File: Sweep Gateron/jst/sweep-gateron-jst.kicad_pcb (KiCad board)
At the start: 2 copper layers, 229.5 x 95.2 mm, 61 parts, among them SW10 SW_Push, SW10_r1 SW_Push, SW11 SW_Push, SW11_r1 SW_Push, SW12 SW_Push, SW12_r1 SW_Push, SW13_r1 SW_Push, SW14 SW_Push, SW14_r1 SW_Push, SW15 SW_Push, SW15_r1 SW_Push, SW16 SW_Push, SW16_r1 SW_Push, SW17 SW_Push, SW18 SW_Push, SW2 SW_Push, SW2 SW_SPDT, SW20 SW_Push, SW21 SW_Push, SW2_r1 SW_Push, SW3 SW_Push, SW3_r1 SW_Push, SW4 SW_Push, SW4_r1 SW_Push, SW5 SW_Push, SW5_r1 SW_Push, SW6 SW_Push, SW6_r1 SW_Push, SW7_r1 SW_Push, SW8 SW_Push, SW8_r1 SW_Push, SW9 SW_Push, SW9_r1 SW_Push, U1 ProMicro-kbd, U2 ProMicro-kbd

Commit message: Added gerber files
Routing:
- net gnd: vias 33 -> 34
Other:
- board text added: "There is no prize to perfection, only an end to pursuit"
- board text removed: "The Aeroplane Flies High (Turns Left, Looks Right)"
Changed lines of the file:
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@@
 		)
 		(fp_text user "RESET"
-			(at 0 2.286 90)
-			(layer "B.SilkS")
+			(at 0 -1.2 90)
+			(layer "F.SilkS")
 			(effects
 				(font
@@
 		)
 		(fp_text user "RESET"
-			(at 0 2.286 90)
-			(layer "B.SilkS")
+			(at 0 1.7 90)
+			(layer "F.SilkS")
 			(effects
 				(font
@@
 	(gr_text "Face down"
 		(at 160.10984 99.23 90)
-		(layer "F.SilkS")
-		(effects
-			(font
-				(size 1.5 1.5)
-				(thickness 0.3)
-			)
-		)
-	)
-	(gr_text "Face down"
-		(at 139.7 99.06 90)
-		(layer "F.SilkS")
+		(layer "B.SilkS")
 		(effects
 			(font
@@
 		)
 	)
-	(gr_text "The Aeroplane Flies High (Turns Left, Looks Right)"
-		(at 233.62984 122.936 0)
+	(gr_text "There is no prize to perfection, only an end to pursuit"
+		(at 232 123 0)
 		(layer "B.SilkS")
 		(effects
@@
 		)
 	)
+	(gr_text "Face down"
+		(at 139.7 99.06 90)
+		(layer "B.SilkS")
+		(effects
+			(font
+				(size 1.5 1.5)
+				(thickness 0.3)
+			)
+		)
+	)
 	(segment
-		(start 158.381843 85.323001)
-		(end 157.231843 84.173001)
+		(start 160.10984 86.585)
+		(end 160.12184 86.573)
+		(width 0.25)
+		(layer "F.Cu")
+		(net 1)
+	)
+	(segment
+		(start 160.10984 88.054)
+		(end 160.10984 86.585)
 		(width 0.25)
 		(layer "F.Cu")
@@
 	)
 	(segment
-		(start 157.231843 84.173001)
-		(end 155.720841 84.173001)
+		(start 157.558842 84.5)
+		(end 156.04784 84.5)
 		(width 0.25)
 		(layer "F.Cu")
@@
 	)
 	(segment
-		(start 155.720841 84.173001)
+		(start 156.04784 84.5)
 		(end 155.02984 83.482)
 		(width 0.25)
@@
 	)
 	(segment
-		(start 160.10984 86.585)
-		(end 160.12184 86.573)
+		(start 159.746841 85.323001)
+		(end 158.381843 85.323001)
 		(width 0.25)
 		(layer "F.Cu")
@@
 	)
 	(segment
-		(start 160.12184 85.698)
-		(end 159.746841 85.323001)
+		(start 159 115.920799)
+		(end 159 92)
 		(width 0.25)
 		(layer "F.Cu")
@@
 	)
 	(segment
-		(start 159.746841 85.323001)
-		(end 158.381843 85.323001)
+		(start 159 92)
+		(end 155.5 88.5)
 		(width 0.25)
 		(layer "F.Cu")
@@
 	)
 	(segment
-		(start 160.10984 88.054)
-		(end 160.10984 86.585)
+		(start 158.381843 85.323001)
+		(end 157.558842 84.5)
 		(width 0.25)
 		(layer "F.Cu")
@@
 	)
 	(segment
-		(start 160.12184 86.573)
-		(end 160.12184 85.698)
+		(start 160.12184 85.698)
+		(end 159.746841 85.323001)
 		(width 0.25)
 		(layer "F.Cu")
@@
 	)
 	(segment
-		(start 155.02984 88.02984)
+		(start 155.5 83.952162)
 		(end 155.02984 83.482002)
 		(width 0.25)
@@
 	)
 	(segment
-		(start 159 115.920799)
-		(end 159 92)
+		(start 155.5 88.5)
+		(end 155.5 83.952162)
 		(width 0.25)
 		(layer "F.Cu")
@@
 	)
 	(segment
-		(start 157.1527 117.768099)
-		(end 159 115.920799)
+		(start 160.12184 86.573)
+		(end 160.12184 85.698)
 		(width 0.25)
 		(layer "F.Cu")
@@
 	)
 	(segment
-		(start 159 92)
-		(end 155.02984 88.02984)
+		(start 157.1527 117.768099)
+		(end 159 115.920799)
 		(width 0.25)
 		(layer "F.Cu")
@@
 		(size 0.8)
 		(drill 0.4)
+		(layers "F.Cu" "B.Cu")
+		(free yes)
+		(net 2)
+	)
+	(via
+		(at 137.5 90)
+		(size 0.8)
+		(drill 0.4)

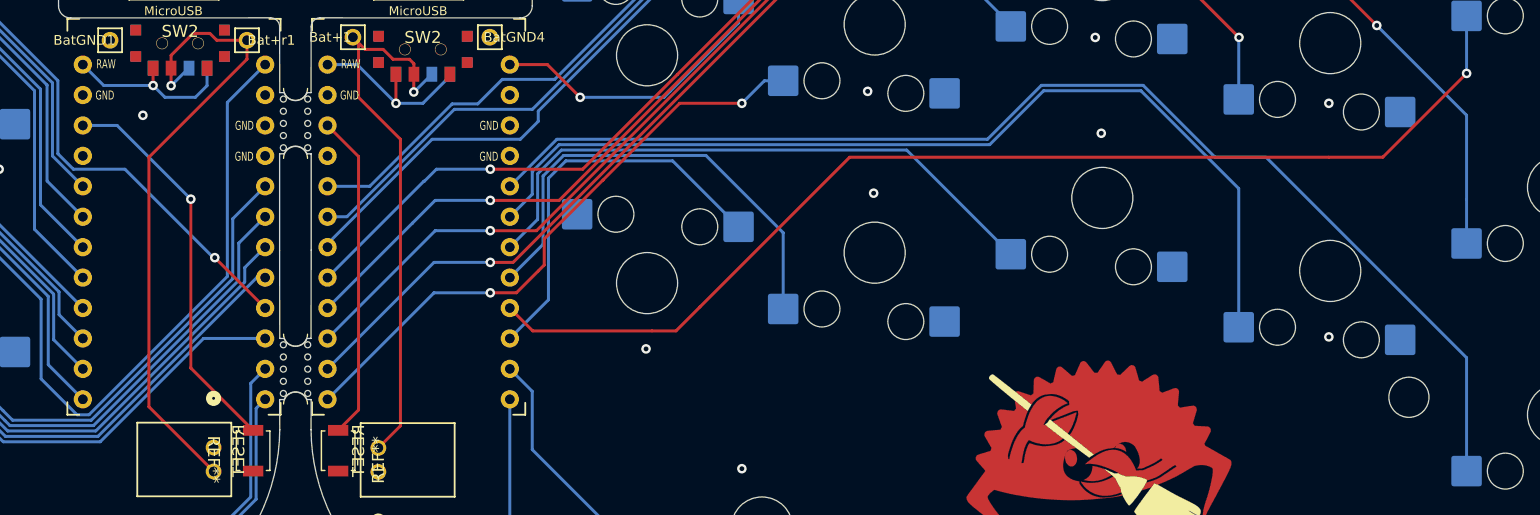
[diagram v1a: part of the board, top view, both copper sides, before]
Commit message: Fixed swapped pads and generated gerber files
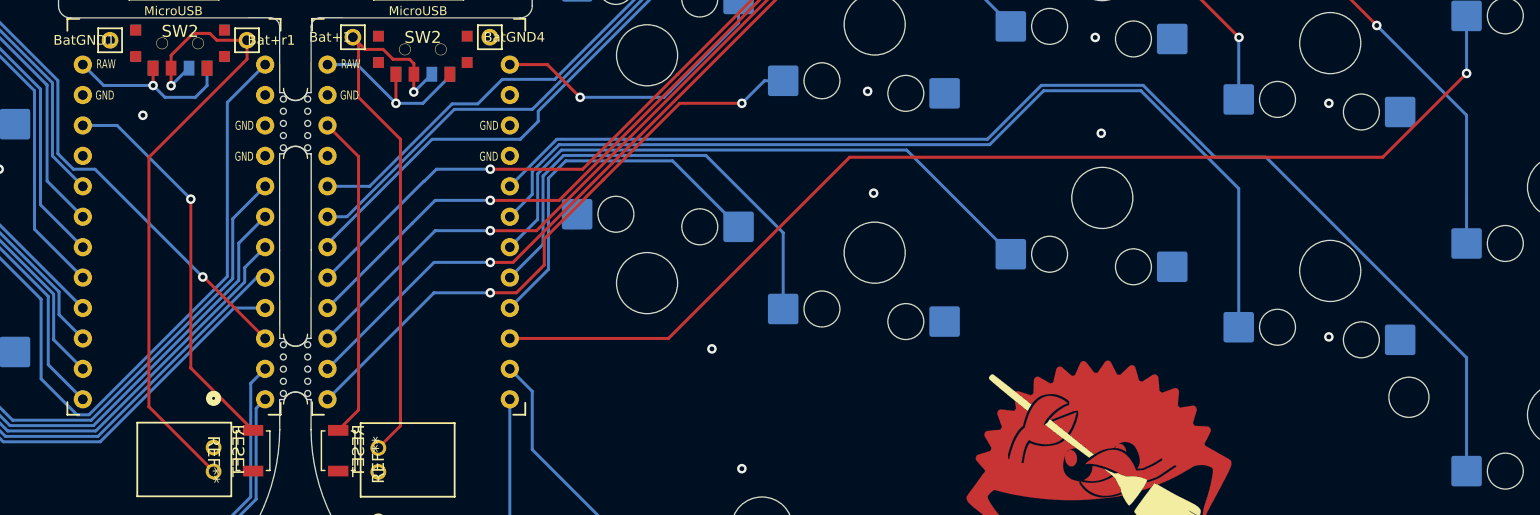
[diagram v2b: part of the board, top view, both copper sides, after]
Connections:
- U1 pad 10: Switch15 -> Switch1
- U1 pad 9: Switch1 -> Switch15
- U2 pad 10: Switch15_r -> Switch1_r
- U2 pad 9: Switch1_r -> Switch15_r
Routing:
- net Switch15_r: track 33.5 -> 30.9 mm
- net Switch1: track 128.1 -> 129.2 mm
- net Switch15: track 41.5 -> 42.5 mm
- net Switch1_r: track 94.4 -> 93.8 mm
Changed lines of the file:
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@@
 			(layers "*.Cu" "B.Mask" "F.SilkS")
 			(remove_unused_layers no)
-			(net 6 "Switch1")
+			(net 20 "Switch15")
 			(pinfunction "D7")
 			(pintype "bidirectional")
@@
 			(layers "*.Cu" "B.Mask" "F.SilkS")
 			(remove_unused_layers no)
-			(net 20 "Switch15")
+			(net 6 "Switch1")
 			(pinfunction "E6")
 			(pintype "bidirectional")
@@
 			(layers "*.Cu" "B.Mask" "F.SilkS")
 			(remove_unused_layers no)
-			(net 36 "Switch1_r")
+			(net 33 "Switch15_r")
 			(pinfunction "D7")
 			(pintype "bidirectional")
@@
 			(layers "*.Cu" "B.Mask" "F.SilkS")
 			(remove_unused_layers no)
-			(net 33 "Switch15_r")
+			(net 36 "Switch1_r")
 			(pinfunction "E6")
 			(pintype "bidirectional")
@@
 	)
 	(via
-		(at 179.5 109.5)
+		(at 185 109.5)
 		(size 0.8)
 		(drill 0.4)
@@
 	)
 	(segment
-		(start 143.5 101.8826)
-		(end 147.7054 106.088)
+		(start 142.5 103.5)
+		(end 142.5774 103.5)
+		(width 0.25)
+		(layer "F.Cu")
+		(net 6)
+	)
+	(segment
+		(start 142.5774 103.5)
+		(end 147.7054 108.628)
 		(width 0.25)
 		(layer "F.Cu")
@@
 	)
 	(via
-		(at 143.5 101.8826)
+		(at 142.5 103.5)
 		(size 0.8)
 		(drill 0.4)
@@
 	)
 	(segment
-		(start 136 94.5)
-		(end 131.69521 94.5)
-		(width 0.25)
-		(layer "B.Cu")
-		(net 6)
-	)
-	(segment
 		(start 61.663082 61.5)
 		(end 52.6375 70.525582)
@@
 	)
 	(segment
+		(start 133.5 94.5)
+		(end 142.5 103.5)
+		(width 0.25)
+		(layer "B.Cu")
+		(net 6)
+	)
+	(segment
 		(start 84.836935 66.5)
 		(end 79.836935 61.5)
@@
 	)
 	(segment
-		(start 143.3826 101.8826)
-		(end 136 94.5)
-		(width 0.25)
-		(layer "B.Cu")
-		(net 6)
-	)
-	(segment
 		(start 130.402 93.20679)
 		(end 130.402 87.10169)
@@
 	)
 	(segment
-		(start 143.5 101.8826)
-		(end 143.3826 101.8826)
+		(start 52.6375 70.525582)
+		(end 52.6375 72.3)
 		(width 0.25)
 		(layer "B.Cu")
@@
 	)
 	(segment
-		(start 52.6375 70.525582)
-		(end 52.6375 72.3)
+		(start 131.69521 94.5)
+		(end 130.402 93.20679)
 		(width 0.25)
 		(layer "B.Cu")
@@
 	(segment
 		(start 131.69521 94.5)
-		(end 130.402 93.20679)
+		(end 133.5 94.5)
 		(width 0.25)
 		(layer "B.Cu")
@@
 	)
 	(segment
-		(start 125.84157 117.255)
-		(end 133.93405 117.255)
+		(start 119.58657 111)
+		(end 125.84157 117.255)
 		(width 0.25)
 		(layer "B.Cu")
@@
 	)
 	(segment
-		(start 115.6345 111)
-		(end 119.58657 111)
+		(start 133.93405 117.255)
+		(end 145.10105 106.088)
 		(width 0.25)
 		(layer "B.Cu")
@@
 	)
 	(segment
-		(start 142.56105 108.628)
-		(end 147.7054 108.628)
+		(start 125.84157 117.255)
+		(end 133.93405 117.255)
 		(width 0.25)
 		(layer "B.Cu")
@@
 	)
 	(segment
-		(start 113.3425 108.708)
-		(end 115.6345 111)
+		(start 115.6345 111)
+		(end 119.58657 111)
 		(width 0.25)
 		(layer "B.Cu")
@@
 	)
 	(segment
-		(start 133.93405 117.255)
-		(end 142.56105 108.628)
+		(start 113.3425 108.708)
+		(end 115.6345 111)
 		(width 0.25)
 		(layer "B.Cu")
@@
 	)
 	(segment
-		(start 119.58657 111)
-		(end 125.84157 117.255)
+		(start 145.10105 106.088)
+		(end 147.7054 106.088)
 		(width 0.25)
 		(layer "B.Cu")
@@
 	)
 	(segment
-		(start 168.12924 108.628)
-		(end 171.353 105.40424)
+		(start 171.353 102.86424)
+		(end 168.12924 106.088)
 		(width 0.25)
 		(layer "B.Cu")
@@
 	)
 	(segment
-		(start 171.353 105.40424)
-		(end 171.353 95.25548)
+		(start 171.353 95.25548)
+		(end 171.353 102.86424)
 		(width 0.25)
 		(layer "B.Cu")
@@
 	)
 	(segment
-		(start 182 108)
-		(end 184 106)
-		(width 0.25)
-		(layer "F.Cu")
-		(net 36)
-	)
-	(segment
-		(start 180 108)
-		(end 182 108)
-		(width 0.25)
-		(layer "F.Cu")
-		(net 36)
-	)
-	(segment
-		(start 168.12924 106.088)
-		(end 170.04124 108)
-		(width 0.25)
-		(layer "F.Cu")
-		(net 36)
-	)
-	(segment
 		(start 241 93.5)
-		(end 248 86.5)
+		(end 196.5 93.5)
 		(width 0.25)
 		(layer "F.Cu")
@@
 	)
 	(segment
-		(start 236.5 93.5)
+		(start 248 86.5)
 		(end 241 93.5)
 		(width 0.25)
@@
 	(segment
 		(start 196.5 93.5)
-		(end 236.5 93.5)
-		(width 0.25)
-		(layer "F.Cu")
-		(net 36)
-	)
-	(segment
-		(start 184 106)
-		(end 196.5 93.5)
+		(end 181.372 108.628)
 		(width 0.25)
 		(layer "F.Cu")
@@
 	)
 	(segment
-		(start 170.04124 108)
-		(end 180 108)
+		(start 181.372 108.628)
+		(end 168.12924 108.628)
 		(width 0.25)
 		(layer "F.Cu")
